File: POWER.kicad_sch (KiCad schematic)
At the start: 85 parts, among them IC9901 ${DEVICE}, IC9902 ${DEVICE}, IC9903 ${DEVICE}, IC9904 ${DEVICE}, IC9905 ${DEVICE}, J9901 ${FAMILY}, J9902 ${FAMILY}, J9903 ${FAMILY}

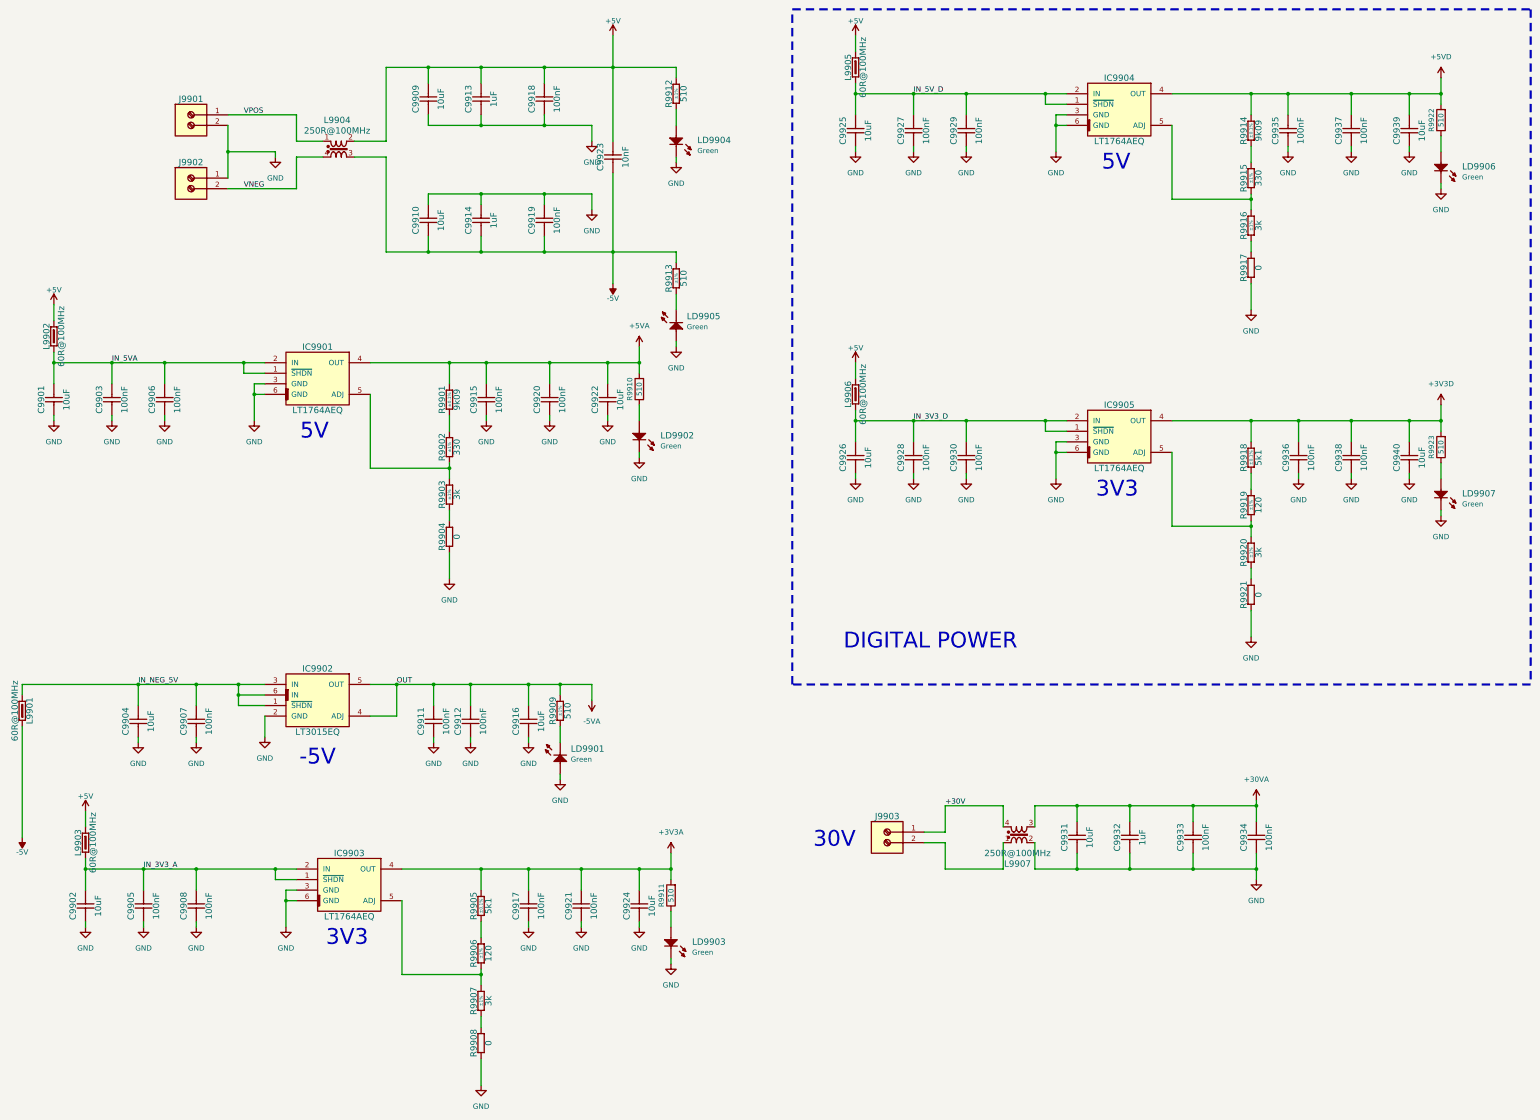
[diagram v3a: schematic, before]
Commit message: Added New LDOs
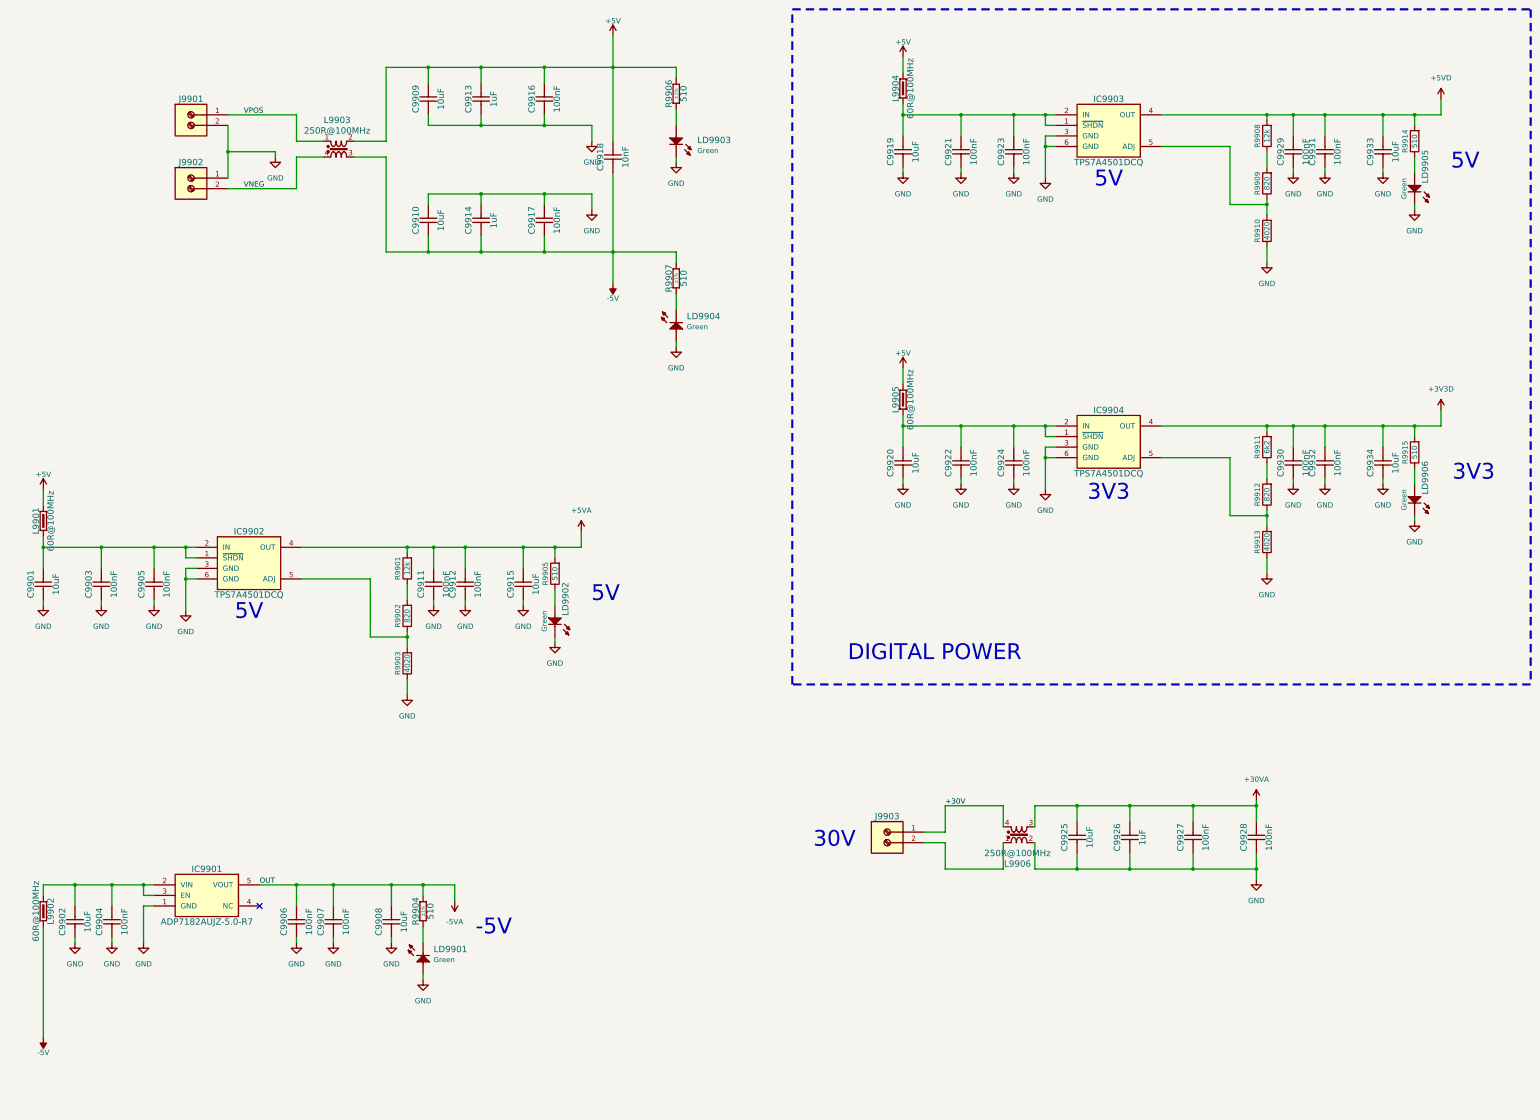
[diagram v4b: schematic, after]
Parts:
- removed C9904, C9916, C9922, C9924, C9925, C9926, C9939, C9940: 10uF, Capacitors SMD:CAPC3216X180N, symbol CERN:Capacitors SMD/CC1206_10UF_50V_10%_X5R
- removed C9908, C9915, C9917, C9920, C9927, C9928, C9935, C9936, C9937, C9938: 100nF, Capacitors SMD:CAPC1608X87N, symbol CERN:Capacitors SMD/CC0603_100NF_50V_10%_X5R
- removed IC9901, IC9903, IC9904, IC9905: ${DEVICE}, ICs And Semiconductors SMD:TO170P1394X457-6N-R900X1060, symbol CERN:Regulators/LT1764AEQ#PBF
- removed IC9902: ${DEVICE}, ICs And Semiconductors SMD:TO170P1394X457-6N-R900X1060, symbol CERN:Regulators/LT3015EQ#PBF
- removed L9903, L9906: 60R@100MHz, Inductors SMD:INDC4516X180N, symbol CERN:Inductors SMD/IND1806_MURATA_BLM41PG600SN1L [alt]
- removed LD9903, LD9907: ${COLOR}, ICs And Semiconductors SMD:LED_KINGBRIGHT_KPH-1608CGCK, symbol CERN:LEDs & Displays/LED_KINGBRIGHT_KPH-1608CGCK
- removed R9901, R9914: 9k09, Resistors SMD:RESC1608X55N, symbol CERN:Resistors SMD/R0603_9K09_0.1%_0.063W_10PPM
- removed R9902, R9915: 330, Resistors SMD:RESC1608X55N, symbol CERN:Resistors SMD/R0603_330R_1%_0.1W_100PPM
- removed R9903, R9907, R9916, R9920: 3k, Resistors SMD:RESC1608X55N, symbol CERN:Resistors SMD/R0603_3K_1%_0.1W_100PPM
- removed R9904, R9908, R9917, R9921: 0, Resistors SMD:RESC1608X55N, symbol CERN:Resistors SMD/R0603_0R_JUMPER
- removed R9905, R9918: 5k1, Resistors SMD:RESC1608X64N, symbol CERN:Resistors SMD/R0603_5K1_0.1%_0.1W_25PPM
- removed R9906, R9919: 120, Resistors SMD:RESC1608X55N, symbol CERN:Resistors SMD/R0603_120R_1%_0.1W_100PPM
- removed R9909: 510, Resistors SMD:RESC1608X55N, symbol CERN:Resistors SMD/R0603_510R_1%_0.1W_100PPM
- removed R9922, R9923: 510, Resistor_SMD:R_0603_1608Metric_Pad0.98x0.95mm_HandSolder, symbol Device:R
- added C9904, C9922, C9923, C9924, C9931, C9932: 100nF, Capacitors SMD:CAPC1608X87N, symbol CERN:Capacitors SMD/CC0603_100NF_50V_10%_X5R
- added C9908, C9915, C9919, C9920, C9933, C9934: 10uF, Capacitors SMD:CAPC3216X180N, symbol CERN:Capacitors SMD/CC1206_10UF_50V_10%_X5R
- added IC9901: ${DEVICE}, ICs And Semiconductors SMD:SOT95P280X90-5N, symbol CERN:Regulators/ADP7182AUJZ-5.0-R7
- added IC9902, IC9903, IC9904: ${DEVICE}, ICs And Semiconductors SMD:SOT127P700X180-6N, symbol CERN:Regulators/TPS7A4501DCQ
- added L9904: 60R@100MHz, Inductors SMD:INDC4516X180N, symbol CERN:Inductors SMD/IND1806_MURATA_BLM41PG600SN1L [alt]
- added LD9905: ${COLOR}, ICs And Semiconductors SMD:LED_KINGBRIGHT_KPH-1608CGCK, symbol CERN:LEDs & Displays/LED_KINGBRIGHT_KPH-1608CGCK
- added R9901, R9908: 12k, Resistor_SMD:R_0603_1608Metric_Pad0.98x0.95mm_HandSolder, symbol Device:R
- added R9902, R9909, R9912: 820, Resistor_SMD:R_0603_1608Metric_Pad0.98x0.95mm_HandSolder, symbol Device:R
- added R9903, R9913: 4020, Resistor_SMD:R_0603_1608Metric_Pad0.98x0.95mm_HandSolder, symbol Device:R
- added R9904: 510, Resistors SMD:RESC1608X55N, symbol CERN:Resistors SMD/R0603_510R_1%_0.1W_100PPM
- added R9905, R9914, R9915: 510, Resistor_SMD:R_0603_1608Metric_Pad0.98x0.95mm_HandSolder, symbol Device:R
- L9901, L9905: Database Name Inductors & Transformers -> (none); Database Table Name Inductors SMD -> (none); Part Number IND1806_MURATA_BLM41PG600SN1L -> (none); Part Number Nocolon IND1806_MURATA_BLM41PG600SN1L [alt] -> (none)
- LD9902, LD9906: Database Name ICs And Semiconductors_Backup -> (none); Database Table Name LEDs & Displays -> (none); Part Number LED_KINGBRIGHT_KPH-1608CGCK -> (none); Part Number Nocolon LED_KINGBRIGHT_KPH-1608CGCK -> (none)
- R9910: value 510 -> 4020
- R9911: value 510 -> 6k2
- renumbered C9918 to C9916, C9919 to C9917, C9923 to C9918, C9931 to C9925, C9932 to C9926, C9933 to C9927, C9934 to C9928, L9904 to L9903, L9907 to L9906, LD9904 to LD9903, LD9905 to LD9904, R9912 to R9906, R9913 to R9907
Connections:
- net IN_3V3_D is gone; now on net +3V3D: C9930.2
- net +3V3D: now also R9911.2, C9932.2, C9934.2, IC9904.4 (OUT), R9915.2
- net +5V: now also L9901.2, L9904.2; no longer L9902.2
- net +5VA: now also C9911.2, C9912.2, C9915.2, IC9902.4 (OUT), R9901.2, R9905.2; no longer R9910.2
- net +5VD: now also C9929.2, C9931.2, C9933.2, IC9903.4 (OUT), R9908.2, R9914.2
- net -5V: now also L9902.2; no longer L9901.2
- net -5VA: now also C9906.2, C9907.2, C9908.2, IC9901.5 (VOUT), R9904.2; no longer C9911.2, C9912.2
- net GND: now also R9910.1, C9904.1, C9908.1, C9915.1, C9919.1, C9920.1, C9922.1, C9923.1, C9924.1, C9931.1, C9932.1, C9933.1, C9934.1, IC9901.1 (GND), IC9902.3 (GND), IC9902.6 (GND), IC9903.3 (GND), IC9903.6 (GND), IC9904.3 (GND), IC9904.6 (GND), LD9905.1 (C), R9903.1, R9913.1
- net at R9911.1: now also R9912.2
- net at LD9901.1 (C): now also R9904.1
- net at LD9902.2 (A): now also R9905.1; no longer R9910.1
- net at LD9906.2 (A): now also R9915.1
- net +3V3A: no longer names the net of C9921.2
- net +3V3A: now also C9919.2, C9923.2, IC9903.1 (~{SHDN}), IC9903.2 (IN), L9904.1; no longer R9911.2
- net IN_3V3_A: no longer names the net of C9902.2
- net IN_3V3_A: now also L9902.1, C9904.2, IC9901.2 (VIN), IC9901.3 (EN); no longer C9905.2
- net IN_5VA: no longer names the net of C9901.2, C9903.2
- net IN_5VA: now also C9905.2, L9901.1, IC9902.1 (~{SHDN}), IC9902.2 (IN); no longer C9906.2, L9902.1
- net IN_5V_D: no longer names the net of L9905.1
- net IN_5V_D: now also C9920.2, C9922.2, C9924.2, IC9904.1 (~{SHDN}), IC9904.2 (IN); no longer C9929.2
- removed net IN_NEG_5V: C9907.2, L9901.1
- new net: R9908.1, R9909.2
- new net: IC9904.5 (ADJ), R9912.1, R9913.2
- new net: IC9903.5 (ADJ), R9909.1, R9910.2
- new net: IC9902.5 (ADJ), R9902.1, R9903.2
- new net: R9901.1, R9902.2
- new net: LD9905.2 (A), R9914.1
- no-connect marks 0 -> 1

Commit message: WIP snapshot
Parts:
- removed C9901, C9902, C9908, C9915: 10uF, Capacitors SMD:CAPC3216X180N, symbol CERN:Capacitors SMD/CC1206_10UF_50V_10%_X5R
- removed C9903, C9904, C9905, C9906, C9907, C9911, C9912: 100nF, Capacitors SMD:CAPC1608X87N, symbol CERN:Capacitors SMD/CC0603_100NF_50V_10%_X5R
- removed IC9901: ${DEVICE}, ICs And Semiconductors SMD:SOT95P280X90-5N, symbol CERN:Regulators/ADP7182AUJZ-5.0-R7
- removed IC9902: ${DEVICE}, ICs And Semiconductors SMD:SOT127P700X180-6N, symbol CERN:Regulators/TPS7A4501DCQ
- removed L9901, L9902: 60R@100MHz, Inductors SMD:INDC4516X180N, symbol CERN:Inductors SMD/IND1806_MURATA_BLM41PG600SN1L [alt]
- removed LD9901, LD9902: ${COLOR}, ICs And Semiconductors SMD:LED_KINGBRIGHT_KPH-1608CGCK, symbol CERN:LEDs & Displays/LED_KINGBRIGHT_KPH-1608CGCK
- removed R9901: 12k, Resistor_SMD:R_0603_1608Metric_Pad0.98x0.95mm_HandSolder, symbol Device:R
- removed R9902: 820, Resistor_SMD:R_0603_1608Metric_Pad0.98x0.95mm_HandSolder, symbol Device:R
- removed R9903: 4020, Resistor_SMD:R_0603_1608Metric_Pad0.98x0.95mm_HandSolder, symbol Device:R
- removed R9904: 510, Resistors SMD:RESC1608X55N, symbol CERN:Resistors SMD/R0603_510R_1%_0.1W_100PPM
- removed R9905: 510, Resistor_SMD:R_0603_1608Metric_Pad0.98x0.95mm_HandSolder, symbol Device:R
- renumbered C9909 to C9901, C9910 to C9902, C9913 to C9903, C9914 to C9904, C9916 to C9905, C9917 to C9906, C9918 to C9907, C9919 to C9908, C9920 to C9909, C9921 to C9910, C9922 to C9911, C9923 to C9912, C9924 to C9913, C9925 to C9914, C9926 to C9915, C9927 to C9916, C9928 to C9917, C9929 to C9918, C9930 to C9919, C9931 to C9920, C9932 to C9921, C9933 to C9922, C9934 to C9923, IC9903 to IC9901, IC9904 to IC9902, L9903 to L9901, L9904 to L9902, L9905 to L9903, L9906 to L9904, LD9903 to LD9901, LD9904 to LD9902, LD9905 to LD9903, LD9906 to LD9904, R9906 to R9901, R9907 to R9902, R9908 to R9903, R9909 to R9904, R9910 to R9905, R9911 to R9906, R9912 to R9907, R9913 to R9908, R9914 to R9909, R9915 to R9910
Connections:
- no-connect marks 1 -> 0
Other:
- note removed: "-5V"

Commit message: Update project files and backups
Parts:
- removed R9903: 12k, Resistor_SMD:R_0603_1608Metric_Pad0.98x0.95mm_HandSolder, symbol Device:R
- removed R9904, R9907: 820, Resistor_SMD:R_0603_1608Metric_Pad0.98x0.95mm_HandSolder, symbol Device:R
- removed R9905, R9908: 4020, Resistor_SMD:R_0603_1608Metric_Pad0.98x0.95mm_HandSolder, symbol Device:R
- removed R9906: 6k2, Resistor_SMD:R_0603_1608Metric_Pad0.98x0.95mm_HandSolder, symbol Device:R
- removed R9909, R9910: 510, Resistor_SMD:R_0603_1608Metric_Pad0.98x0.95mm_HandSolder, symbol Device:R
- added C9924, C9925: 10uF, Capacitors SMD:CAPC3216X180N, symbol CERN:Capacitors SMD/CC1206_10UF_50V_10%_X5R
- added IC9903: ${DEVICE}, ICs And Semiconductors SMD:TO254P1405X457-4N-R889X1067, symbol CERN_Linux:Regulators/LT1085IM
- added LD9905: ${COLOR}, ICs And Semiconductors SMD:LED_KINGBRIGHT_KPH-1608CGCK, symbol CERN:LEDs & Displays/LED_KINGBRIGHT_KPH-1608CGCK
- added R9903, R9905, R9906, R9915: 4k7, Resistors SMD:RESC1608X55N, symbol CERN:Resistors SMD/R0603_4K7_1%_0.1W_100PPM
- added R9904: 10k, Resistors SMD:RESC1608X55N, symbol CERN:Resistors SMD/R0603_10K_1%_0.1W_100PPM
- added R9907: 8k2, Resistors SMD:RESC1608X55N, symbol CERN:Resistors SMD/R0603_8K2_1%_0.1W_100PPM
- added R9908, R9909, R9910, R9911, R9912, R9913: 510, Resistors SMD:RESC1608X55N, symbol CERN:Resistors SMD/R0603_510R_1%_0.1W_100PPM
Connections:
- net +30VA: now also R9915.2
- net +3V3D: now also R9907.2, R9909.2
- net +5V: now also C9924.2, IC9903.3 (IN)
- net +5VD: now also R9903.1, R9908.2
- net GND: now also C9924.1, C9925.1, LD9905.1 (C), R9905.2, R9906.2, R9913.1
- net at LD9904.2 (A): now also R9909.1
- net at IC9902.5 (ADJ): now also R9906.1, R9907.1
- net at IC9901.5 (ADJ): now also R9904.1, R9905.1
- net at LD9903.2 (A): now also R9908.1
- new net: R9912.1, R9913.2
- new net: R9911.1, R9912.2
- new net: IC9903.1 (ADJ), R9910.1, R9911.2
- new net: LD9905.2 (A), R9915.1
- new net: R9903.2, R9904.2
- new net +3V6: C9925.2, IC9903.2 (OUT), IC9903.4 (OUT), R9910.2
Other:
- note added: "PLL power dropper"
- note added: "R1 = 14k7 R2 = 4k7 VOut = 4.99V"
- note added: "R1 = 8k2 R2 = 4k7 VOut = 3.32V"
- note added: "Vout = 1.25 * (300 / 100) = 3.75V Iout = 1A, PTot = ~2 W"
